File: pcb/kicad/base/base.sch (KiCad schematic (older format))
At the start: 35 parts, among them P1 J-Link SWD, P2 SMA, P3 Power Source, P4 USB Micro B, U1 SAMB11G18A-edit, Y1 32.768kHz, Y2 26MHz

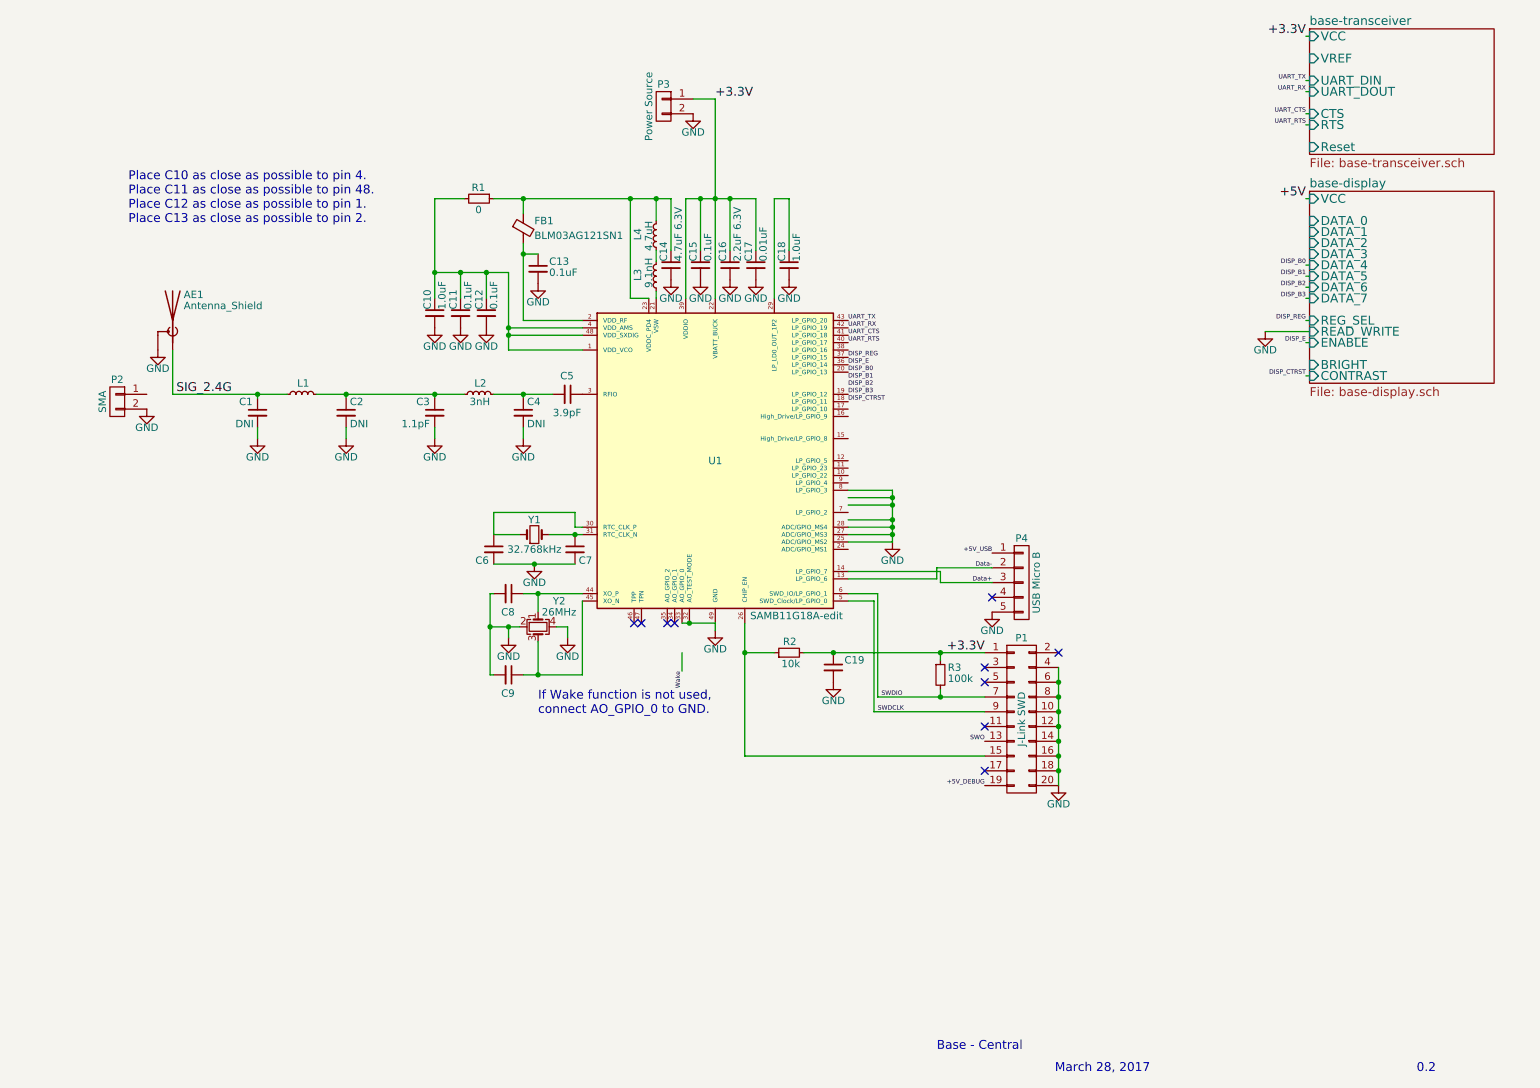
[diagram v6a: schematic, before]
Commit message: Update display and XBee position once more
GPIO pins were rearranged to achieve a tighter fit on the available
components. Patch antenna is now replaced with SMA connector for first
prototype. Buttons will be simulated with a pin header short. Audio
speaker is planned to go below the display, perhpas on the side of the
housing.
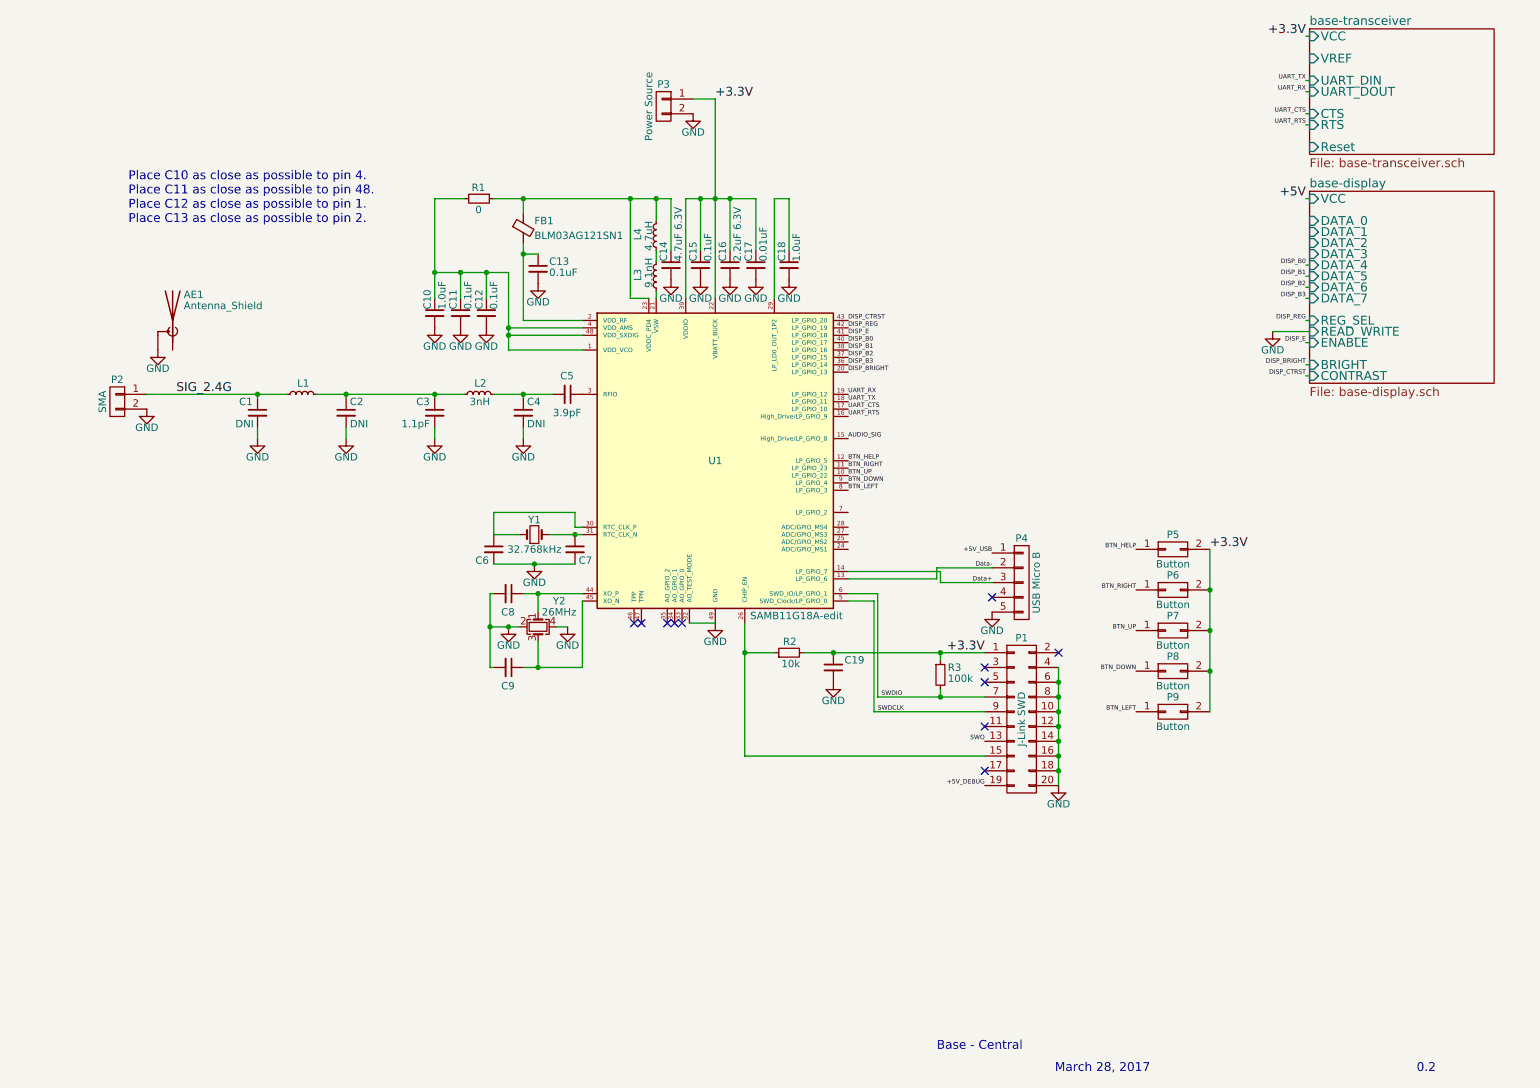
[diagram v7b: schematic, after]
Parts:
- added P5, P6, P7, P8, P9: Button, Misc:Socket_Strip_Straight_1x02_Pitch2.54mm_Drill0.64mm, symbol CONN_02X01
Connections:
- net labels added: AUDIO_SIG, BTN_DOWN, BTN_HELP, BTN_LEFT, BTN_RIGHT, BTN_UP, DISP_BRIGHT
- net labels removed: Wake
- wire segments 105 -> 94
- no-connect marks 10 -> 11
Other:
- note removed: "If Wake function is not used,\nconnect AO_GPIO_0 to GND."
- moved on the sheet: C9
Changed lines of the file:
@@
 L GND #PWR01
 U 1 1 58BA111C
-P 5850 4650
-F 0 "#PWR01" H 5850 4400 50  0001 C CNN
-F 1 "GND" H 5850 4525 50  0000 C CNN
-F 2 "" H 5850 4650 50  0000 C CNN
-F 3 "" H 5850 4650 50  0000 C CNN
-	1    5850 4650
+P 5850 4600
+F 0 "#PWR01" H 5850 4350 50  0001 C CNN
+F 1 "GND" H 5850 4475 50  0000 C CNN
+F 2 "" H 5850 4600 50  0000 C CNN
+F 3 "" H 5850 4600 50  0000 C CNN
+	1    5850 4600
 	1    0    0    -1
 $EndComp
@@
 Text Label 7675 5400 2    30   ~ 0
 SWO
-Text Label 6750 2700 0    30   ~ 0
+Text Label 6750 3200 0    30   ~ 0
 UART_RTS
-Text Label 6750 2650 0    30   ~ 0
+Text Label 6750 3150 0    30   ~ 0
 UART_CTS
-Text Label 5625 4925 3    30   ~ 0
-Wake
-Text Notes 4650 5225 0    60   ~ 0
-If Wake function is not used,\nconnect AO_GPIO_0 to GND.
 $Sheet
 S 9875 575  1250 850
@@
 L GND #PWR019
 U 1 1 58BE3DF0
-P 4850 4700
-F 0 "#PWR019" H 4850 4450 50  0001 C CNN
-F 1 "GND" H 4850 4575 50  0000 C CNN
-F 2 "" H 4850 4700 50  0000 C CNN
-F 3 "" H 4850 4700 50  0000 C CNN
-	1    4850 4700
+P 4850 4625
+F 0 "#PWR019" H 4850 4375 50  0001 C CNN
+F 1 "GND" H 4850 4500 50  0000 C CNN
+F 2 "" H 4850 4625 50  0000 C CNN
+F 3 "" H 4850 4625 50  0000 C CNN
+	1    4850 4625
 	1    0    0    -1
 $EndComp
@@
 L GND #PWR020
 U 1 1 58BE3F81
-P 4450 4700
-F 0 "#PWR020" H 4450 4450 50  0001 C CNN
-F 1 "GND" H 4450 4575 50  0000 C CNN
-F 2 "" H 4450 4700 50  0000 C CNN
-F 3 "" H 4450 4700 50  0000 C CNN
-	1    4450 4700
+P 4450 4625
+F 0 "#PWR020" H 4450 4375 50  0001 C CNN
+F 1 "GND" H 4450 4500 50  0000 C CNN
+F 2 "" H 4450 4625 50  0000 C CNN
+F 3 "" H 4450 4625 50  0000 C CNN
+	1    4450 4625
 	1    0    0    -1
 $EndComp
@@
 L C_Small C9
 U 1 1 58BE4649
-P 4450 4950
-F 0 "C9" V 4575 4900 50  0000 L CNN
-F 1 "C_Small" H 4460 4870 50  0001 L CNN
-F 2 "Capacitors_SMD:C_0402" H 4450 4950 50  0001 C CNN
-F 3 "" H 4450 4950 50  0000 C CNN
-	1    4450 4950
+P 4450 4900
+F 0 "C9" V 4575 4850 50  0000 L CNN
+F 1 "C_Small" H 4460 4820 50  0001 L CNN
+F 2 "Capacitors_SMD:C_0402" H 4450 4900 50  0001 C CNN
+F 3 "" H 4450 4900 50  0000 C CNN
+	1    4450 4900
 	0    1    1    0
 $EndComp
@@
 NoConn ~ 5525 4600
 NoConn ~ 5575 4600
-Text Label 6750 2550 0    30   ~ 0
+Text Label 6750 3100 0    30   ~ 0
 UART_TX
+Text Label 6750 3050 0    30   ~ 0
+UART_RX
+Text Label 6750 2700 0    30   ~ 0
+DISP_B0
+Text Label 6750 2750 0    30   ~ 0
+DISP_B1
+Text Label 6750 2800 0    30   ~ 0
+DISP_B2
+Text Label 6750 2850 0    30   ~ 0
+DISP_B3
+Text Label 6750 2650 0    30   ~ 0
+DISP_E
 Text Label 6750 2600 0    30   ~ 0
-UART_RX
-Text Label 6750 2900 0    30   ~ 0
-DISP_B0
-Text Label 6750 2950 0    30   ~ 0
-DISP_B1
-Text Label 6750 3000 0    30   ~ 0
-DISP_B2
-Text Label 6750 3050 0    30   ~ 0
-DISP_B3
-$Comp
-L GND #PWR022
-U 1 1 58C42CEE
-P 7050 4050
-F 0 "#PWR022" H 7050 3800 50  0001 C CNN
-F 1 "GND" H 7050 3925 50  0000 C CNN
-F 2 "" H 7050 4050 50  0000 C CNN
-F 3 "" H 7050 4050 50  0000 C CNN
-	1    7050 4050
-	1    0    0    -1
-$EndComp
-$Comp
-L SAMB11G18A-edit U1
-U 1 1 58C5ED8B
-P 5850 3500
-F 0 "U1" H 5850 3500 50  0000 C CNN
-F 1 "SAMB11G18A-edit" H 6400 2450 50  0000 C CNN
-F 2 "QFN-48-1EP_6x6mm_Pitch0.4mm" H 6800 2375 50  0001 C CIN
-F 3 "" H 5850 3500 50  0000 C CNN
-	1    5850 3500
-	1    0    0    -1
-$EndComp
-Text Label 6750 2850 0    30   ~ 0
-DISP_E
-Text Label 6750 2800 0    30   ~ 0
 DISP_REG
 $Comp
@@
 $EndComp
 $Comp
-L GND #PWR023
+L GND #PWR022
 U 1 1 58E322FD
 P 2075 2750
-F 0 "#PWR023" H 2075 2500 50  0001 C CNN
+F 0 "#PWR022" H 2075 2500 50  0001 C CNN
 F 1 "GND" H 2075 2625 50  0000 C CNN
 F 2 "" H 2075 2750 50  0000 C CNN
@@
 $EndComp
 $Comp
-L GND #PWR024
+L GND #PWR023
 U 1 1 58E5D85A
-P 9575 2625
-F 0 "#PWR024" H 9575 2375 50  0001 C CNN
-F 1 "GND" H 9575 2500 50  0000 C CNN
-F 2 "" H 9575 2625 50  0000 C CNN
-F 3 "" H 9575 2625 50  0000 C CNN
-	1    9575 2625
+P 9625 2625
+F 0 "#PWR023" H 9625 2375 50  0001 C CNN
+F 1 "GND" H 9625 2500 50  0000 C CNN
+F 2 "" H 9625 2625 50  0000 C CNN
+F 3 "" H 9625 2625 50  0000 C CNN
+	1    9625 2625
 	1    0    0    -1
 $EndComp
 Text Label 7675 5700 2    30   ~ 0
 +5V_DEBUG
-Text Label 6750 3100 0    30   ~ 0
-DISP_CTRST
+Text Label 6750 2900 0    30   ~ 0
+DISP_BRIGHT
 Text Label 9850 2925 2    30   ~ 0
 DISP_CTRST
@@
 +5V_USB
 $Comp
-L GND #PWR?
+L GND #PWR024
 U 1 1 58E83B3B
 P 7725 4525
-F 0 "#PWR?" H 7725 4275 50  0001 C CNN
+F 0 "#PWR024" H 7725 4275 50  0001 C CNN
 F 1 "GND" H 7725 4400 50  0000 C CNN
 F 2 "" H 7725 4525 50  0000 C CNN
@@
 Wire Wire Line
 	2750 3350 2750 3275
-Wire Wire Line
-	5850 4600 5850 4650
 Connection ~ 5275 1725
 Wire Wire Line
@@
 	2750 3050 2750 3075
 Wire Wire Line
-	2175 3050 2950 3050
+	2000 3050 2950 3050
 Wire Wire Line
 	3350 3075 3350 3050
@@
 	9875 1225 9850 1225
 Wire Wire Line
-	4775 4625 4850 4625
-Wire Wire Line
-	4850 4625 4850 4700
-Wire Wire Line
-	4450 4700 4450 4625
-Wire Wire Line
-	4325 4625 4525 4625
-Wire Wire Line
-	4550 4950 4950 4950
-Wire Wire Line
-	4650 4950 4650 4725
-Connection ~ 4450 4625
-Wire Wire Line
-	4325 4950 4350 4950
-Wire Wire Line
-	4325 4400 4325 4950
+	4550 4900 4950 4900
+Wire Wire Line
+	4650 4900 4650 4725
+Wire Wire Line
+	4325 4900 4350 4900
+Wire Wire Line
+	4325 4400 4325 4900
 Connection ~ 4325 4625
 Wire Wire Line
@@
 	4650 4525 4650 4400
 Connection ~ 4650 4400
-Connection ~ 4650 4950
-Wire Wire Line
-	4950 4950 4950 4450
+Connection ~ 4650 4900
+Wire Wire Line
+	4950 4900 4950 4450
 Wire Wire Line
 	4350 4200 4900 4200
@@
 	5850 1050 5700 1050
 Wire Wire Line
-	5625 4600 5850 4600
-Connection ~ 5675 4600
-Wire Wire Line
-	5625 4800 5625 4925
-Wire Wire Line
-	2175 2750 2175 3050
-Wire Wire Line
-	7050 3800 6750 3800
-Wire Wire Line
-	7050 3700 7050 4050
-Wire Wire Line
-	7050 4050 6750 4050
-Wire Wire Line
-	6750 4000 7050 4000
-Connection ~ 7050 4000
-Wire Wire Line
-	7050 3950 6750 3950
-Connection ~ 7050 3950
-Wire Wire Line
-	7050 3900 6750 3900
-Connection ~ 7050 3900
-Wire Wire Line
 	9850 2925 9875 2925
 Wire Wire Line
@@
 	9875 2700 9850 2700
 Wire Wire Line
-	9575 2625 9875 2625
+	9625 2625 9875 2625
 Wire Wire Line
 	9850 2400 9875 2400
@@
 	9850 1725 9875 1725
 Wire Wire Line
-	6750 3750 7050 3750
-Connection ~ 7050 3800
-Wire Wire Line
-	6750 3700 7050 3700
-Connection ~ 7050 3750
-Wire Wire Line
 	6750 4300 7350 4300
 Wire Wire Line
@@
 Wire Wire Line
 	7375 4325 7725 4325
+Text Label 9850 2850 2    30   ~ 0
+DISP_BRIGHT
+Wire Wire Line
+	9850 2850 9875 2850
+Wire Wire Line
+	5675 4600 5850 4600
+$Comp
+L CONN_02X01 P5
+U 1 1 58E891CA
+P 8950 4100
+F 0 "P5" H 8950 4200 50  0000 C CNN
+F 1 "Button" H 8950 4000 50  0000 C CNN
+F 2 "Misc:Socket_Strip_Straight_1x02_Pitch2.54mm_Drill0.64mm" H 8950 2900 50  0001 C CNN
+F 3 "" H 8950 2900 50  0000 C CNN
+	1    8950 4100
+	1    0    0    -1
+$EndComp
+Text Label 9200 4100 0    60   ~ 0
++3.3V
+Text Label 6750 2550 0    30   ~ 0
+DISP_CTRST
+Text Label 6750 3350 0    30   ~ 0
+AUDIO_SIG
+Wire Wire Line
+	4775 4625 4850 4625
+Wire Wire Line
+	4325 4625 4525 4625
+Connection ~ 4450 4625
+$Comp
+L SAMB11G18A-edit U1
+U 1 1 58C5ED8B
+P 5850 3500
+F 0 "U1" H 5850 3500 50  0000 C CNN
+F 1 "SAMB11G18A-edit" H 6400 2450 50  0000 C CNN
+F 2 "QFN-48-1EP_6x6mm_Pitch0.4mm" H 6800 2375 50  0001 C CIN
+F 3 "" H 5850 3500 50  0000 C CNN
+	1    5850 3500
+	1    0    0    -1
+$EndComp
+NoConn ~ 5625 4600
+$Comp
+L CONN_02X01 P7
+U 1 1 58ED6A9B
+P 8950 4650
+F 0 "P7" H 8950 4750 50  0000 C CNN
+F 1 "Button" H 8950 4550 50  0000 C CNN
+F 2 "Misc:Socket_Strip_Straight_1x02_Pitch2.54mm_Drill0.64mm" H 8950 3450 50  0001 C CNN
+F 3 "" H 8950 3450 50  0000 C CNN
+	1    8950 4650
+	1    0    0    -1
+$EndComp
+$Comp
+L CONN_02X01 P6
+U 1 1 58ED6BB6
+P 8950 4375
+F 0 "P6" H 8950 4475 50  0000 C CNN
+F 1 "Button" H 8950 4275 50  0000 C CNN
+F 2 "Misc:Socket_Strip_Straight_1x02_Pitch2.54mm_Drill0.64mm" H 8950 3175 50  0001 C CNN
+F 3 "" H 8950 3175 50  0000 C CNN
+	1    8950 4375
+	1    0    0    -1
+$EndComp
+$Comp
+L CONN_02X01 P8
+U 1 1 58ED7110
+P 8950 4925
+F 0 "P8" H 8950 5025 50  0000 C CNN
+F 1 "Button" H 8950 4825 50  0000 C CNN
+F 2 "Misc:Socket_Strip_Straight_1x02_Pitch2.54mm_Drill0.64mm" H 8950 3725 50  0001 C CNN
+F 3 "" H 8950 3725 50  0000 C CNN
+	1    8950 4925
+	1    0    0    -1
+$EndComp
+$Comp
+L CONN_02X01 P9
+U 1 1 58ED7A7A
+P 8950 5200
+F 0 "P9" H 8950 5300 50  0000 C CNN
+F 1 "Button" H 8950 5100 50  0000 C CNN
+F 2 "Misc:Socket_Strip_Straight_1x02_Pitch2.54mm_Drill0.64mm" H 8950 4000 50  0001 C CNN
+F 3 "" H 8950 4000 50  0000 C CNN
+	1    8950 5200
+	1    0    0    -1
+$EndComp
+Wire Wire Line
+	9200 4100 9200 5200
+Connection ~ 9200 4375
+Connection ~ 9200 4650
+Connection ~ 9200 4925
+Text Label 8700 4100 2    30   ~ 0
+BTN_HELP
+Text Label 8700 4375 2    30   ~ 0
+BTN_RIGHT
+Text Label 8700 4650 2    30   ~ 0
+BTN_UP
+Text Label 8700 4925 2    30   ~ 0
+BTN_DOWN
+Text Label 8700 5200 2    30   ~ 0
+BTN_LEFT
+Text Label 6750 3500 0    30   ~ 0
+BTN_HELP
+Text Label 6750 3550 0    30   ~ 0
+BTN_RIGHT
+Text Label 6750 3600 0    30   ~ 0
+BTN_UP
+Text Label 6750 3650 0    30   ~ 0
+BTN_DOWN
+Text Label 6750 3700 0    30   ~ 0
+BTN_LEFT
 $EndSCHEMATC
